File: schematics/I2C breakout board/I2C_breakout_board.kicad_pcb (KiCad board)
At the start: 2 copper layers, 22 parts, among them J1 Conn_01x01_Pin, J10 Conn_01x01_Pin, J11 Conn_01x01_Pin, J12 Conn_01x01_Pin, J13 Conn_01x01_Pin, J14 Conn_01x01_Pin, J15 Conn_01x01_Pin, J16 Conn_01x01_Pin, J17 Conn_01x01_Pin, J2 Conn_01x01_Pin, J3 Conn_01x01_Pin, J4 Conn_01x01_Pin, J5 Conn_01x01_Pin, J6 Conn_01x01_Pin, J7 Conn_01x01_Pin, J8 Conn_01x01_Pin, J9 Conn_01x01_Pin, U1 ENS210-LQFM, U2 OPT4001DTSR

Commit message: updated schematic
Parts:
- removed J10, J11, J12, J13, J14, J15, J16, J17, J3, J4, J5, J6, J7, J8, J9: Conn_01x01_Pin, Connector_PinHeader_2.54mm:PinHeader_1x01_P2.54mm_Vertical
- J1, J2: value Conn_01x01_Pin -> Conn_01x07_Pin; footprint Connector_PinHeader_2.54mm:PinHeader_1x01_P2.54mm_Vertical -> Connector_PinHeader_2.54mm:PinHeader_1x07_P2.54mm_Vertical
- moved U1 52.4 mm to (153.5, 141.5)
- moved C1 49.3 mm to (153.3, 135.1), turned to 0 degrees
- moved U2 45.0 mm to (153.4, 145.0)
- moved J2 43.5 mm to (148.6, 131.3)
- moved J1 41.4 mm to (144.0, 131.3)
- moved C2 33.6 mm to (153.3, 138.2), turned to 0 degrees
- moved U3 14.8 mm to (155.3, 131.4)
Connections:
- C1 pad 2: GND -> U3_GND
- C2 pad 1: GND -> U3_GND
- J1 pad 1: Net-(J1-Pin_1) -> +3.3V
- J2 pad 1: +3.3V -> U3_GND
- U1 pad 2: Net-(J1-Pin_1) -> SCL
- U1 pad 3: Net-(J17-Pin_1) -> SDA
- U1 pad 4: GND -> U3_GND
- U1 pad 5: GND -> U3_GND
- U2 pad 2: Net-(J6-Pin_1) -> U2_ADDR
- U2 pad 3: Net-(J13-Pin_1) -> unconnected-(U2-NC-Pad3)
- U2 pad 4: GND -> U3_GND
- U2 pad 5: Net-(J4-Pin_1) -> SCL
- U2 pad 6: Net-(J12-Pin_1) -> unconnected-(U2-NC-Pad6)
- U2 pad 7: Net-(J11-Pin_1) -> U2_INT
- U2 pad 8: Net-(J5-Pin_1) -> SDA
- U3 pad 1: Net-(J7-Pin_1) -> U3_RO
- U3 pad 2: Net-(J8-Pin_1) -> U3_/RE
- U3 pad 3: Net-(J9-Pin_1) -> U3_DE
- U3 pad 4: Net-(J10-Pin_1) -> U3_DI
- U3 pad 5: GND -> U3_GND
- U3 pad 6: Net-(J15-Pin_1) -> U3_A
- U3 pad 7: Net-(J14-Pin_1) -> U3__B

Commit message: finalized PCB for breakout board
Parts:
- C1, C2: moved to B.Cu
- moved U1 26.9 mm to (130.8, 127.0), turned to 90 degrees
- moved C1 26.5 mm to (128.2, 127.0), turned to 90 degrees
- moved U2 26.1 mm to (130.8, 132.1)
- moved C2 25.9 mm to (128.2, 132.1), turned to 90 degrees
- moved U3 25.5 mm to (130.8, 138.4), turned to -90 degrees
- moved J1 20.1 mm to (124.5, 127.0)
- moved J2 12.3 mm to (137.2, 127.0)
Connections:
- J1 pad 2: SCL -> U3_GND
- J1 pad 3: U2_ADDR -> U2_INT
- J2 pad 1: U3_GND -> SDA
- J2 pad 2: SDA -> SCL
- J2 pad 3: U2_INT -> U2_ADDR
- J2 pad 4: U3__B -> +3.3V
- J2 pad 5: U3_A -> U3__B
- J2 pad 6: U3_GND -> U3_A
- J2 pad 7: +3.3V -> U3_GND
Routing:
- net U3_GND: track 0.00 -> 32.9 mm, vias 0 -> 5
- net +3.3V: track 0.00 -> 29.9 mm, vias 0 -> 3
- net SDA: track 0.00 -> 13.6 mm, vias 0 -> 1
- net SCL: track 0.00 -> 13.4 mm
- net U2_INT: track 0.00 -> 9.11 mm
- net U3_DI: track 0.00 -> 8.90 mm, vias 0 -> 1
- net U2_ADDR: track 0.00 -> 8.88 mm
- net U3_/RE: track 0.00 -> 8.75 mm
- net U3_RO: track 0.00 -> 8.75 mm
- net U3_A: track 0.00 -> 8.63 mm
- net U3__B: track 0.00 -> 8.62 mm
- net U3_DE: track 0.00 -> 8.61 mm
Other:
- board outline added: 18.8 x 21.3 mm
- board text added: "3v3"
- board text added: "A"
- board text added: "ADR"
- board text added: "B"
- board text added: "DE"
- board text added: "DI"
- board text added: "GND"
- board text added: "INT"
- board text added: "RO"
- board text added: "SCL"
- board text added: "SDA"
- board text added: "~{RE}"

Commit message: first commit for soil sensor board
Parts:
- J1, J2: moved to B.Cu
- turned J1 to 180 degrees
- turned J2 to 180 degrees
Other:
- board size 18.8 x 21.3 mm -> 16.3 x 19.6 mm

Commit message: final version of air sensors breakout board
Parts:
- removed J1, J2: Conn_01x07_Pin, Connector_PinHeader_2.54mm:PinHeader_1x07_P2.54mm_Vertical
- added C3: 0.1u, Capacitor_SMD:C_0805_2012Metric_Pad1.18x1.45mm_HandSolder, B.Cu at (143.5, 90.4)
- added J3: 54602-908LF, 54602_908LF_footprints:CONN8_2-908LF_AMP, F.Cu at (139.1, 97.2)
- added J4: Conn_01x05_Pin, Connector_PinHeader_2.54mm:PinHeader_1x05_P2.54mm_Vertical, B.Cu at (137.2, 71.1)
- added J5: Conn_01x05_Pin, Connector_PinHeader_2.54mm:PinHeader_1x05_P2.54mm_Vertical, B.Cu at (149.9, 81.3)
- added R1: 120, Resistor_SMD:R_0805_2012Metric_Pad1.20x1.40mm_HandSolder, F.Cu at (143.5, 90.4)
- moved C2 61.0 mm to (143.5, 73.0), turned to 0 degrees
- moved U1 57.9 mm to (143.5, 70.5), turned to 180 degrees
- moved U2 55.4 mm to (143.5, 78.1), turned to -90 degrees
- moved U3 55.2 mm to (143.5, 84.7)
- moved C1 53.6 mm to (143.5, 75.6), turned to 180 degrees
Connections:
- net U3_GND renamed GND
- U3 pad 6: U3_A -> Net-(U3-A)
- U3 pad 7: U3__B -> Net-(U3-B)
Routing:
- net GND: track 32.9 -> 8.05 mm, vias 5 -> 3
- net +3.3V: track 29.9 -> 7.09 mm
- net Net-(U3-B): track 0.00 -> 10.0 mm
- net U3_A: track 8.63 -> 0.00 mm
- net U3__B: track 8.62 -> 0.00 mm
- net Net-(U3-A): track 0.00 -> 7.50 mm
- net SDA: track 13.6 -> 19.9 mm, vias 1 -> 2
- net SCL: track 13.4 -> 18.3 mm, vias 0 -> 2
- net U3_DI: track 8.90 -> 5.61 mm, vias 1 -> 0
- net U3_RO: track 8.75 -> 5.61 mm
- net U2_ADDR: track 8.88 -> 6.89 mm
- net U2_INT: track 9.11 -> 8.16 mm
- net U3_DE: track 8.61 -> 7.74 mm
- net U3_/RE: track 8.75 -> 9.45 mm
- added copper zone on B.Cu, net +3.3V
- added copper zone on B.Cu, net GND
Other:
- board size 16.3 x 19.6 mm -> 17.8 x 43.2 mm
- board text added: "3V3"
- board text removed: "3v3"
- board text removed: "A"
- board text removed: "B"

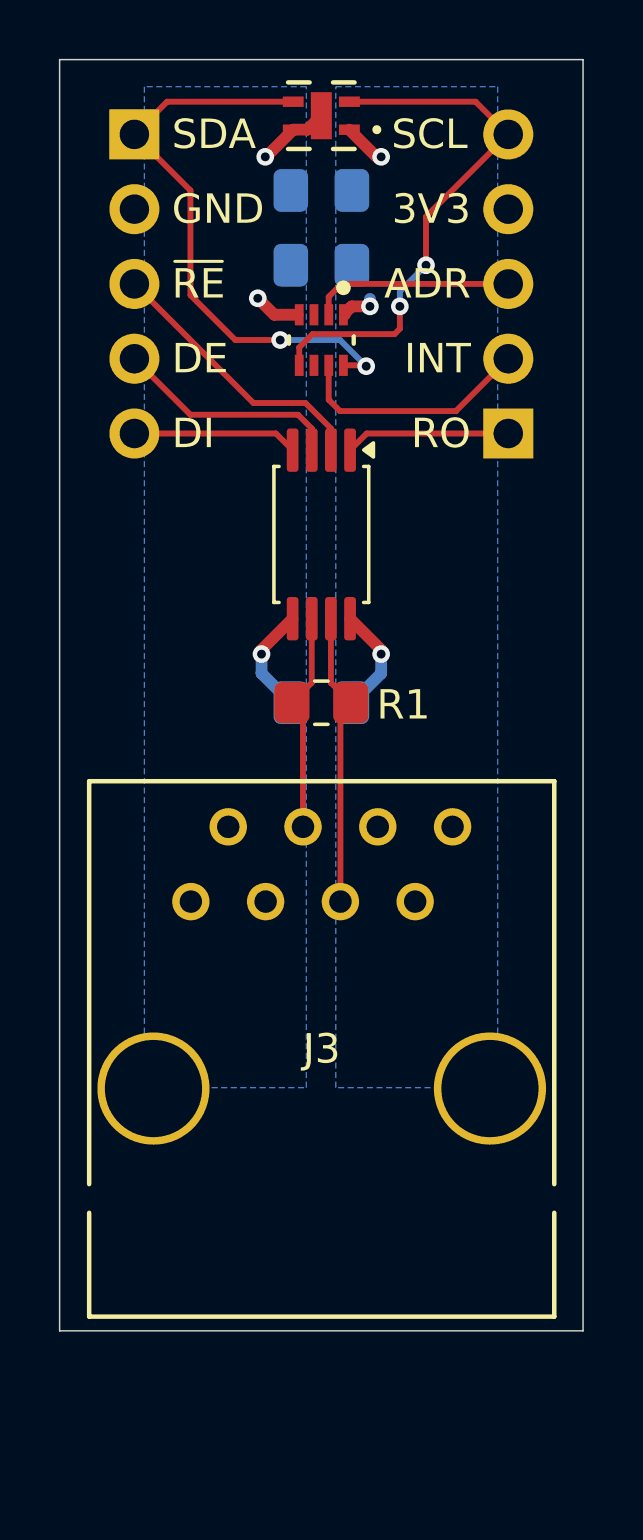
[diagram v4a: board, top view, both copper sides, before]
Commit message: added PMOS to turn off power to RJ45 connector
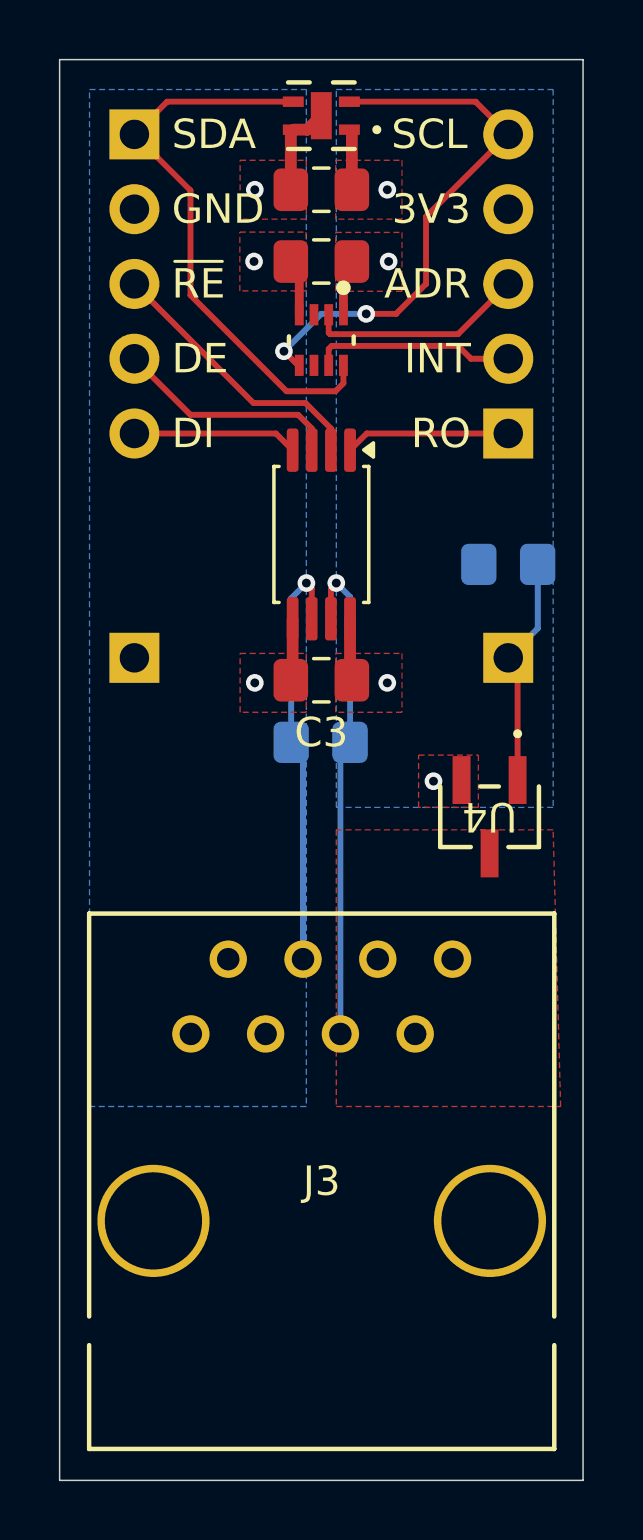
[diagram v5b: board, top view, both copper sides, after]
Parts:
- added J1: Conn_01x01_Pin, Connector_PinHeader_2.54mm:PinHeader_1x01_P2.54mm_Vertical, B.Cu at (149.9, 88.9)
- added J2: Conn_01x01_Pin, Connector_PinHeader_2.54mm:PinHeader_1x01_P2.54mm_Vertical, B.Cu at (137.2, 88.9)
- added R2: 100k, Resistor_SMD:R_0805_2012Metric_Pad1.20x1.40mm_HandSolder, B.Cu at (149.9, 85.7)
- added U4: AO3401A, AO3401A_footprints:SOT-23-3L_AOS-M, F.Cu at (149.2, 94.3)
- C1, C2, C3: moved to F.Cu
- R1: moved to B.Cu
- moved J3 4.50 mm to (139.1, 101.7)
- moved R1 1.35 mm to (143.5, 91.8)
- moved C3 0.76 mm to (143.5, 89.7)
- moved C1 0.13 mm to (143.5, 75.4)
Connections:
- J3 pad 7: +3.3V -> Net-(U4-D)
- J3 pad 8: +3.3V -> Net-(U4-D)
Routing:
- net Net-(J1-Pin_1): track 0.00 -> 7.87 mm
- net Net-(U3-A): track 7.50 -> 14.4 mm, vias 0 -> 1
- net Net-(U3-B): track 10.0 -> 16.9 mm, vias 0 -> 1
- net U2_ADDR: track 6.89 -> 8.20 mm
- net U2_INT: track 8.16 -> 6.88 mm
- net +3.3V: track 7.09 -> 6.28 mm, vias 3 -> 4
- net GND: track 8.05 -> 7.36 mm
- net SDA: track 19.9 -> 19.4 mm, vias 2 -> 0
- added copper zone on F.Cu, net +3.3V
- added copper zone on F.Cu, net GND
- added copper zone on F.Cu, net Net-(U4-D)
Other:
- board size 17.8 x 43.2 mm -> 17.8 x 48.3 mm

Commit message: Final changes to pcbs before ordering
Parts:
- renumbered J4 to J1, J5 to J2, J1 to J4, J2 to J5, U4 to Q1
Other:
- board text added: "Add I2C pullups"
- board text added: "U3"
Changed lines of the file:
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@@
 		(filling no)
 		(pcbplotparams
-			(layerselection 0x00000000_00000000_55555555_5755f5ff)
+			(layerselection 0x00000000_00000000_55555555_575555ff)
 			(plot_on_all_layers_selection 0x00000000_00000000_00000000_00000000)
 			(disableapertmacros no)
@@
 			(outputformat 1)
 			(mirror no)
-			(drillshape 1)
+			(drillshape 0)
 			(scaleselection 1)
-			(outputdirectory "")
+			(outputdirectory "C:/Users/shelj/Downloads/gerber_i2cboard/")
 		)
 	)
@@
 		(at 149.225 94.2975 180)
 		(tags "AO3401A ")
-		(property "Reference" "U4"
-			(at 0 0 180)
+		(property "Reference" "Q1"
+			(at 2.667 0.0635 180)
 			(unlocked yes)
 			(layer "F.SilkS")
@@
 			(size 0.6096 1.6256)
 			(layers "F.Cu" "F.Mask" "F.Paste")
-			(net "Net-(J1-Pin_1)")
+			(net "Net-(J4-Pin_1)")
 			(pinfunction "G_1")
 			(pintype "unspecified")
@@
 			(size 0.6096 1.6256)
 			(layers "F.Cu" "F.Mask" "F.Paste")
-			(net "Net-(U4-D)")
+			(net "Net-(Q1-D)")
 			(pinfunction "D_3")
 			(pintype "unspecified")
@@
 		(tags "54602-908LF ")
 		(property "Reference" "J3"
-			(at 4.445 5.004 0)
+			(at -1.1557 -5.156 0)
 			(unlocked yes)
 			(layer "F.SilkS")
@@
 		)
 		(property "Value" "54602-908LF"
-			(at 4.445 5.004 0)
+			(at 4.1783 3.988 0)
 			(unlocked yes)
 			(layer "F.Fab")
@@
 			(layers "*.Cu" "*.Mask")
 			(remove_unused_layers no)
-			(net "Net-(U4-D)")
+			(net "Net-(Q1-D)")
 			(pinfunction "7_7")
 			(pintype "unspecified")
@@
 			(layers "*.Cu" "*.Mask")
 			(remove_unused_layers no)
-			(net "Net-(U4-D)")
+			(net "Net-(Q1-D)")
 			(pinfunction "8_8")
 			(pintype "unspecified")
@@
 		(descr "Through hole straight pin header, 1x05, 2.54mm pitch, single row")
 		(tags "Through hole pin header THT 1x05 2.54mm single row")
-		(property "Reference" "J4"
+		(property "Reference" "J1"
 			(at 0 2.38 0)
 			(layer "B.SilkS")
@@
 			(layers "B.Cu" "B.Mask" "B.Paste")
 			(roundrect_rratio 0.208333)
-			(net "Net-(J1-Pin_1)")
+			(net "Net-(J4-Pin_1)")
 			(pintype "passive")
 		)
@@
 		(descr "Through hole straight pin header, 1x05, 2.54mm pitch, single row")
 		(tags "Through hole pin header THT 1x05 2.54mm single row")
-		(property "Reference" "J5"
+		(property "Reference" "J2"
 			(at 0 2.38 0)
 			(layer "B.SilkS")
@@
 		(descr "Through hole straight pin header, 1x01, 2.54mm pitch, single row")
 		(tags "Through hole pin header THT 1x01 2.54mm single row")
-		(property "Reference" "J1"
+		(property "Reference" "J4"
 			(at 0 2.38 0)
 			(layer "B.SilkS")
@@
 			(layers "*.Cu" "*.Mask")
 			(remove_unused_layers no)
-			(net "Net-(J1-Pin_1)")
+			(net "Net-(J4-Pin_1)")
 			(pinfunction "Pin_1_1")
 			(pintype "passive")
@@
 		(descr "Through hole straight pin header, 1x01, 2.54mm pitch, single row")
 		(tags "Through hole pin header THT 1x01 2.54mm single row")
-		(property "Reference" "J2"
+		(property "Reference" "J5"
 			(at 0 2.38 0)
 			(layer "B.SilkS")
@@
 			(layers "*.Cu" "*.Mask")
 			(remove_unused_layers no)
-			(net "unconnected-(J2-Pin_1-Pad1)")
+			(net "unconnected-(J5-Pin_1-Pad1)")
 			(pinfunction "Pin_1_1")
 			(pintype "passive")
@@
 		)
 	)
+	(gr_text "Add I2C\npullups"
+		(at 138.0744 93.1672 0)
+		(layer "F.SilkS")
+		(effects
+			(font
+				(size 1 1)
+				(thickness 0.1)
+			)
+		)
+	)
 	(gr_text "SCL"
 		(at 148.48 71.12 0)
@@
 		)
 	)
+	(gr_text "U3\n"
+		(at 140.97 84.836 90)
+		(layer "F.SilkS")
+		(effects
+			(font
+				(size 1 1)
+				(thickness 0.1)
+			)
+		)
+	)
 	(segment
 		(start 144.260001 75.725499)
@@
 		(width 0.2)
 		(layer "F.Cu")
-		(net "Net-(J1-Pin_1)")
+		(net "Net-(J4-Pin_1)")
 	)
 	(segment
@@
 		(width 0.2)
 		(layer "F.Cu")
-		(net "Net-(J1-Pin_1)")
+		(net "Net-(J4-Pin_1)")
 	)
 	(segment
@@
 		(width 0.2)
 		(layer "B.Cu")
-		(net "Net-(J1-Pin_1)")
+		(net "Net-(J4-Pin_1)")
 	)
 	(segment
@@
 		(width 0.2)
 		(layer "B.Cu")
-		(net "Net-(J1-Pin_1)")
+		(net "Net-(J4-Pin_1)")
 	)
 	(segment
@@
 	)
 	(zone
-		(net "Net-(U4-D)")
+		(net "Net-(Q1-D)")
 		(layer "F.Cu")
 		(name "3v3_out")
